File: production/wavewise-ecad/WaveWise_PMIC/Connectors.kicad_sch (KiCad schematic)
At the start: 32 parts, among them J1 24V output, J10 5031590200, J11 5031590200, J13 Screw_Terminal_01x03, J2 Conn_01x06_Pin, J3 Conn_01x03_Pin, J5 5031590400, J6 5031590400, J8 5031590800, J9 5031590300

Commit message: fix drc
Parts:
- removed J1: 24V output, Unchecked:2pinmolex, symbol Connector:Screw_Terminal_01x02
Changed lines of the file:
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@@
-    (stroke (width 0) (type default))
-  )
-  (wire (pts (xy 67.31 113.665) (xy 69.215 113.665))
     (stroke (width 0) (type default))
   )
@@
   )
   (wire (pts (xy 68.58 27.94) (xy 80.645 27.94))
-    (stroke (width 0) (type default))
-  )
-  (wire (pts (xy 67.31 111.125) (xy 73.025 111.125))
     (stroke (width 0) (type default))
   )
@@
     )
   )
-  (symbol (lib_id "power:GND") (at 69.215 113.665 0) (unit 1)
-    (in_bom yes) (on_board yes) (dnp no)
-    (property "Reference" "#PWR03" (at 69.215 120.015 0)
-      (effects (font (size 1.27 1.27)) hide)
-    )
-    (property "Value" "GND" (at 72.39 114.3 0)
-      (effects (font (size 1.27 1.27)))
-    )
-    (property "Footprint" "" (at 69.215 113.665 0)
-      (effects (font (size 1.27 1.27)) hide)
-    )
-    (property "Datasheet" "" (at 69.215 113.665 0)
-      (effects (font (size 1.27 1.27)) hide)
-    )
-    (pin "1")
-    (instances
-      (project "WaveWise_PMIC"
-        (path "/8343c01b-8940-4cb8-a17d-91fd7fb1cccd/7fd42481-dc5a-4ae0-adec-c5e7a3228be9"
-          (reference "#PWR03") (unit 1)
-        )
-      )
-    )
-  )
   (symbol (lib_id "power:GND") (at 97.79 148.59 0) (unit 1)
     (in_bom yes) (on_board yes) (dnp no) (fields_autoplaced)
@@
         (path "/8343c01b-8940-4cb8-a17d-91fd7fb1cccd/7fd42481-dc5a-4ae0-adec-c5e7a3228be9"
           (reference "#PWR055") (unit 1)
-        )
-      )
-    )
-  )
-  (symbol (lib_id "Connector:Screw_Terminal_01x02") (at 62.23 113.665 180) (unit 1)
-    (in_bom yes) (on_board yes) (dnp no) (fields_autoplaced)
-    (property "Reference" "J1" (at 62.23 105.41 0)
-      (effects (font (size 1.27 1.27)))
-    )
-    (property "Value" "24V output" (at 62.23 107.95 0)
-      (effects (font (size 1.27 1.27)))
-    )
-    (property "Footprint" "Unchecked:2pinmolex" (at 62.23 113.665 0)
-      (effects (font (size 1.27 1.27)) hide)
-    )
-    (property "Datasheet" "~" (at 62.23 113.665 0)
-      (effects (font (size 1.27 1.27)) hide)
-    )
-    (pin "1")
-    (pin "2")
-    (instances
-      (project "WaveWise_PMIC"
-        (path "/8343c01b-8940-4cb8-a17d-91fd7fb1cccd/7fd42481-dc5a-4ae0-adec-c5e7a3228be9"
-          (reference "J1") (unit 1)
         )
       )
@@
         )
       )
-    )
-  )
-  (symbol (lib_id "power:+24V") (at 73.025 111.125 0) (unit 1)
-    (in_bom yes) (on_board yes) (dnp no) (fields_autoplaced)
-    (property "Reference" "#PWR01" (at 73.025 114.935 0)
-      (effects (font (size 1.27 1.27)) hide)
-    )
-    (property "Value" "+24V" (at 73.025 106.045 0)
-      (effects (font (size 1.27 1.27)))
-    )
-    (property "Footprint" "" (at 73.025 111.125 0)
-      (effects (font (size 1.27 1.27)) hide)
-    )
-    (property "Datasheet" "" (at 73.025 111.125 0)
-      (effects (font (size 1.27 1.27)) hide)
-    )
-    (pin "1")
-    (instances
-      (project "WaveWise_PMIC"
-        (path "/8343c01b-8940-4cb8-a17d-91fd7fb1cccd/7fd42481-dc5a-4ae0-adec-c5e7a3228be9"
-          (reference "#PWR01") (unit 1)
-        )
-      )

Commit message: power stuff
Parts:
- removed R25, R26: 0, Resistor_SMD:R_0805_2012Metric, symbol Device:R
- J5: footprint Unchecked:4pinmolex -> Connector_Molex:Molex_Micro-Fit_3.0_43650-0400_1x04_P3.00mm_Horizontal
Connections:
- net Inverter_Input: now also J13.2 (Pin_2)
- net air_comp_dio renamed SICO_PUMP_CONTROL
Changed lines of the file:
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@@
   (junction (at 50.8 136.144) (diameter 0) (color 0 0 0 0)
-  )
-  (junction (at 44.45 63.5) (diameter 0) (color 0 0 0 0)
   )
   (junction (at 157.48 106.68) (diameter 0) (color 0 0 0 0)
@@
     (stroke (width 0) (type default))
   )
-  (wire (pts (xy 44.45 62.23) (xy 44.45 63.5))
-    (stroke (width 0) (type default))
-  )
   (wire (pts (xy 157.48 111.76) (xy 157.48 106.68))
     (stroke (width 0) (type default))
@@
     (stroke (width 0.15) (type dash))
   )
-  (wire (pts (xy 27.94 63.5) (xy 44.45 63.5))
+  (wire (pts (xy 27.94 63.5) (xy 34.29 63.5))
     (stroke (width 0) (type default))
   )
@@
   )
   (wire (pts (xy 67.31 62.23) (xy 80.01 62.23))
-    (stroke (width 0) (type default))
-  )
-  (wire (pts (xy 44.45 63.5) (xy 44.45 67.31))
     (stroke (width 0) (type default))
   )
@@
     )
   )
-  (global_label "air_comp_dio" (shape input) (at 127 33.02 180) (fields_autoplaced)
-    (effects (font (size 1.27 1.27)) (justify right))
-    (property "Intersheetrefs" "${INTERSHEET_REFS}" (at 111.5569 33.02 0)
-      (effects (font (size 1.27 1.27)) (justify right) hide)
-    )
-  )
-  (global_label "air_comp_dio" (shape input) (at 44.45 74.93 270) (fields_autoplaced)
-    (effects (font (size 1.27 1.27)) (justify right))
-    (property "Intersheetrefs" "${INTERSHEET_REFS}" (at 44.45 90.3731 90)
-      (effects (font (size 1.27 1.27)) (justify right) hide)
-    )
-  )
   (global_label "panel_sense" (shape input) (at 120.904 88.9 180) (fields_autoplaced)
     (effects (font (size 1.27 1.27)) (justify right))
@@
     (effects (font (size 1.27 1.27)) (justify left))
   )
-  (hierarchical_label "Inverter_Input" (shape input) (at 44.45 54.61 90) (fields_autoplaced)
+  (hierarchical_label "Inverter_Input" (shape input) (at 34.29 63.5 0) (fields_autoplaced)
     (effects (font (size 1.27 1.27)) (justify left))
   )
   (hierarchical_label "BATT_SENSE_DIO" (shape input) (at 135.128 63.754 0) (fields_autoplaced)
     (effects (font (size 1.27 1.27)) (justify left))
+  )
+  (hierarchical_label "SICO_PUMP_CONTROL" (shape input) (at 127 33.02 180) (fields_autoplaced)
+    (effects (font (size 1.27 1.27)) (justify right))
   )
   (hierarchical_label "SWDIO" (shape input) (at 34.29 151.13 0) (fields_autoplaced)
@@
     )
   )
-  (symbol (lib_id "power:+5V") (at 40.64 36.83 270) (unit 1)
-    (in_bom yes) (on_board yes) (dnp no) (fields_autoplaced)
-    (property "Reference" "#PWR04" (at 36.83 36.83 0)
-      (effects (font (size 1.27 1.27)) hide)
-    )
-    (property "Value" "+5V" (at 44.45 36.83 90)
-      (effects (font (size 1.27 1.27)) (justify left))
-    )
-    (property "Footprint" "" (at 40.64 36.83 0)
-      (effects (font (size 1.27 1.27)) hide)
-    )
-    (property "Datasheet" "" (at 40.64 36.83 0)
-      (effects (font (size 1.27 1.27)) hide)
-    )
-    (pin "1")
-    (instances
-      (project "WaveWise_PMIC"
-        (path "/8343c01b-8940-4cb8-a17d-91fd7fb1cccd/7fd42481-dc5a-4ae0-adec-c5e7a3228be9"
-          (reference "#PWR04") (unit 1)
-        )
-      )
-    )
-  )
   (symbol (lib_id "2pinmolex:5031590200") (at 31.75 104.14 180) (unit 1)
     (in_bom yes) (on_board yes) (dnp no) (fields_autoplaced)
@@
     )
   )
-  (symbol (lib_id "Device:R") (at 44.45 58.42 180) (unit 1)
-    (in_bom yes) (on_board yes) (dnp yes) (fields_autoplaced)
-    (property "Reference" "R26" (at 46.99 57.15 0)
-      (effects (font (size 1.27 1.27)) (justify right))
-    )
-    (property "Value" "0" (at 46.99 59.69 0)
-      (effects (font (size 1.27 1.27)) (justify right))
-    )
-    (property "Footprint" "Resistor_SMD:R_0805_2012Metric" (at 46.228 58.42 90)
-      (effects (font (size 1.27 1.27)) hide)
-    )
-    (property "Datasheet" "~" (at 44.45 58.42 0)
-      (effects (font (size 1.27 1.27)) hide)
-    )
-    (pin "1")
-    (pin "2")
-    (instances
-      (project "WaveWise_PMIC"
-        (path "/8343c01b-8940-4cb8-a17d-91fd7fb1cccd/7fd42481-dc5a-4ae0-adec-c5e7a3228be9"
-          (reference "R26") (unit 1)
-        )
-      )
-    )
-  )
   (symbol (lib_id "power:GND") (at 27.94 66.04 0) (unit 1)
     (in_bom yes) (on_board yes) (dnp no) (fields_autoplaced)
@@
       (effects (font (size 1.524 1.524)))
     )
-    (property "Footprint" "Unchecked:4pinmolex" (at 29.21 132.08 0)
+    (property "Footprint" "Connector_Molex:Molex_Micro-Fit_3.0_43650-0400_1x04_P3.00mm_Horizontal" (at 29.21 132.08 0)
       (effects (font (size 1.27 1.27) italic) hide)
     )
@@
     )
   )
-  (symbol (lib_id "Device:R") (at 44.45 71.12 180) (unit 1)
-    (in_bom yes) (on_board yes) (dnp no) (fields_autoplaced)
-    (property "Reference" "R25" (at 46.99 69.85 0)
-      (effects (font (size 1.27 1.27)) (justify right))
-    )
-    (property "Value" "0" (at 46.99 72.39 0)
-      (effects (font (size 1.27 1.27)) (justify right))
-    )
-    (property "Footprint" "Resistor_SMD:R_0805_2012Metric" (at 46.228 71.12 90)
-      (effects (font (size 1.27 1.27)) hide)
-    )
-    (property "Datasheet" "~" (at 44.45 71.12 0)
-      (effects (font (size 1.27 1.27)) hide)
-    )
-    (pin "1")
-    (pin "2")
-    (instances
-      (project "WaveWise_PMIC"
-        (path "/8343c01b-8940-4cb8-a17d-91fd7fb1cccd/7fd42481-dc5a-4ae0-adec-c5e7a3228be9"
-          (reference "R25") (unit 1)
-        )
-      )
+  (symbol (lib_id "power:+5V") (at 40.64 36.83 270) (unit 1)
+    (in_bom yes) (on_board yes) (dnp no) (fields_autoplaced)
+    (property "Reference" "#PWR01" (at 36.83 36.83 0)
+      (effects (font (size 1.27 1.27)) hide)
+    )
+    (property "Value" "+5V" (at 44.45 36.83 90)
+      (effects (font (size 1.27 1.27)) (justify left))
+    )
+    (property "Footprint" "" (at 40.64 36.83 0)
+      (effects (font (size 1.27 1.27)) hide)
+    )
+    (property "Datasheet" "" (at 40.64 36.83 0)
+      (effects (font (size 1.27 1.27)) hide)
+    )
+    (pin "1")
+    (instances
+      (project "WaveWise_PMIC"
+        (path "/8343c01b-8940-4cb8-a17d-91fd7fb1cccd/7fd42481-dc5a-4ae0-adec-c5e7a3228be9"
+          (reference "#PWR01") (unit 1)
+        )
+      )

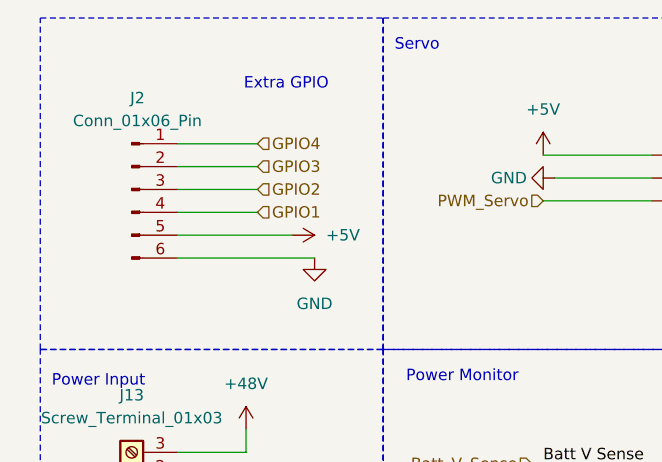
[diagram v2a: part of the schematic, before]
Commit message: change pins on pico for layout
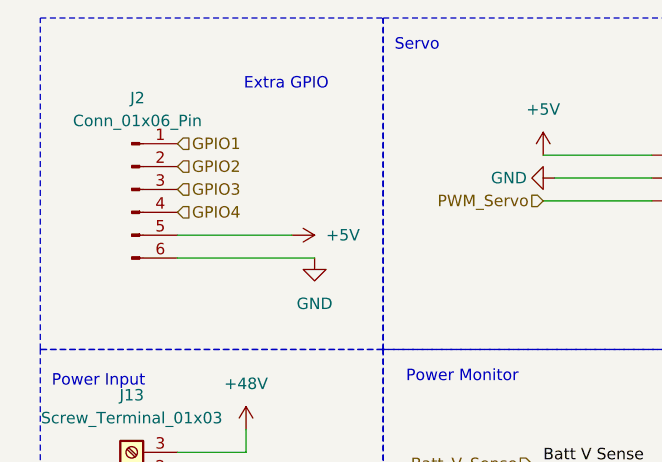
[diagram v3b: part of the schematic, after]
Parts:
- J10, J11: footprint Unchecked:2pinmolex -> Connector_Molex:Molex_MicroClasp_55932-0210_1x02_P2.00mm_Vertical
- J6: footprint Unchecked:4pinmolex -> Connector_Molex:Molex_MicroClasp_55932-0410_1x04_P2.00mm_Vertical
- J8: footprint Unchecked:8pinmolex -> Connector_Molex:Molex_MicroClasp_55932-0810_1x08_P2.00mm_Vertical
- J9: footprint Unchecked:3pinmolex -> Connector_Molex:Molex_MicroClasp_55932-0310_1x03_P2.00mm_Vertical
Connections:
- net GPIO1: now also J2.1 (Pin_1); no longer J2.4 (Pin_4)
- net GPIO2: now also J2.2 (Pin_2); no longer J2.3 (Pin_3)
- net GPIO3: now also J2.3 (Pin_3); no longer J2.2 (Pin_2)
- net GPIO4: now also J2.4 (Pin_4); no longer J2.1 (Pin_1)
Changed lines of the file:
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@@
   (junction (at 157.48 106.68) (diameter 0) (color 0 0 0 0)
-  )
-  (wire (pts (xy 27.94 26.67) (xy 36.83 26.67))
-    (stroke (width 0) (type default))
   )
   (polyline (pts (xy 105.41 123.19) (xy 105.41 126.746))
@@
     (stroke (width 0) (type default))
   )
-  (wire (pts (xy 27.94 31.75) (xy 36.83 31.75))
-    (stroke (width 0) (type default))
-  )
   (wire (pts (xy 124.714 22.098) (xy 124.714 22.86))
     (stroke (width 0) (type default))
@@
     (stroke (width 0) (type default))
   )
-  (wire (pts (xy 27.94 34.29) (xy 36.83 34.29))
-    (stroke (width 0) (type default))
-  )
   (wire (pts (xy 172.72 106.68) (xy 176.53 106.68))
     (stroke (width 0) (type default))
@@
   )
   (wire (pts (xy 120.904 92.71) (xy 128.27 92.71))
-    (stroke (width 0) (type default))
-  )
-  (wire (pts (xy 27.94 29.21) (xy 36.83 29.21))
     (stroke (width 0) (type default))
   )
@@
     )
   )
-  (hierarchical_label "GPIO4" (shape input) (at 36.83 26.67 0) (fields_autoplaced)
+  (hierarchical_label "GPIO4" (shape input) (at 27.94 34.29 0) (fields_autoplaced)
     (effects (font (size 1.27 1.27)) (justify left))
   )
@@
     (effects (font (size 1.27 1.27)) (justify left))
   )
-  (hierarchical_label "GPIO1" (shape input) (at 36.83 34.29 0) (fields_autoplaced)
+  (hierarchical_label "GPIO1" (shape input) (at 27.94 26.67 0) (fields_autoplaced)
     (effects (font (size 1.27 1.27)) (justify left))
   )
-  (hierarchical_label "GPIO3" (shape input) (at 36.83 29.21 0) (fields_autoplaced)
+  (hierarchical_label "GPIO3" (shape input) (at 27.94 31.75 0) (fields_autoplaced)
     (effects (font (size 1.27 1.27)) (justify left))
   )
@@
     (effects (font (size 1.27 1.27)) (justify left))
   )
-  (hierarchical_label "GPIO2" (shape input) (at 36.83 31.75 0) (fields_autoplaced)
+  (hierarchical_label "GPIO2" (shape input) (at 27.94 29.21 0) (fields_autoplaced)
     (effects (font (size 1.27 1.27)) (justify left))
   )
@@
       (effects (font (size 1.524 1.524)))
     )
-    (property "Footprint" "Unchecked:2pinmolex" (at 31.75 104.14 0)
+    (property "Footprint" "Connector_Molex:Molex_MicroClasp_55932-0210_1x02_P2.00mm_Vertical" (at 31.75 104.14 0)
       (effects (font (size 1.27 1.27) italic) hide)
     )
@@
       (effects (font (size 1.524 1.524)))
     )
-    (property "Footprint" "Unchecked:4pinmolex" (at 125.73 116.84 0)
+    (property "Footprint" "Connector_Molex:Molex_MicroClasp_55932-0410_1x04_P2.00mm_Vertical" (at 125.73 116.84 0)
       (effects (font (size 1.27 1.27) italic) hide)
     )
@@
       (effects (font (size 1.524 1.524)) (justify left))
     )
-    (property "Footprint" "Unchecked:8pinmolex" (at 127 22.86 0)
+    (property "Footprint" "Connector_Molex:Molex_MicroClasp_55932-0810_1x08_P2.00mm_Vertical" (at 127 22.86 0)
       (effects (font (size 1.27 1.27) italic) hide)
     )
@@
       (effects (font (size 1.524 1.524)))
     )
-    (property "Footprint" "Unchecked:2pinmolex" (at 31.115 85.725 0)
+    (property "Footprint" "Connector_Molex:Molex_MicroClasp_55932-0210_1x02_P2.00mm_Vertical" (at 31.115 85.725 0)
       (effects (font (size 1.27 1.27) italic) hide)
     )
@@
       (effects (font (size 1.524 1.524)) (justify left))
     )
-    (property "Footprint" "Unchecked:3pinmolex" (at 80.645 27.94 0)
+    (property "Footprint" "Connector_Molex:Molex_MicroClasp_55932-0310_1x03_P2.00mm_Vertical" (at 80.645 27.94 0)
       (effects (font (size 1.27 1.27) italic) hide)
     )

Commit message: add back in 24V output
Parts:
- added J1: 5031590200, Connector_Molex:Molex_MicroClasp_55932-0210_1x02_P2.00mm_Vertical, symbol 2pinmolex:5031590200
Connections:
- net +24V: now also J1.2
- net GND: now also J1.1
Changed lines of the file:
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@@
     (stroke (width 0.15) (type dash))
+  )
+  (wire (pts (xy 71.12 100.33) (xy 78.74 100.33))
+    (stroke (width 0) (type default))
   )
   (wire (pts (xy 27.94 63.5) (xy 34.29 63.5))
@@
     (stroke (width 0) (type default))
   )
+  (wire (pts (xy 71.12 102.87) (xy 74.93 102.87))
+    (stroke (width 0) (type default))
+  )
   (wire (pts (xy 35.56 58.42) (xy 35.56 60.96))
     (stroke (width 0) (type default))
@@
   )
   (wire (pts (xy 38.735 80.645) (xy 38.735 83.185))
+    (stroke (width 0) (type default))
+  )
+  (wire (pts (xy 78.74 97.79) (xy 78.74 100.33))
     (stroke (width 0) (type default))
   )
@@
         (path "/8343c01b-8940-4cb8-a17d-91fd7fb1cccd/7fd42481-dc5a-4ae0-adec-c5e7a3228be9"
           (reference "#PWR01") (unit 1)
+        )
+      )
+    )
+  )
+  (symbol (lib_id "2pinmolex:5031590200") (at 71.12 102.87 180) (unit 1)
+    (in_bom yes) (on_board yes) (dnp no) (fields_autoplaced)
+    (property "Reference" "J1" (at 62.23 93.345 0)
+      (effects (font (size 1.524 1.524)))
+    )
+    (property "Value" "5031590200" (at 62.23 95.885 0)
+      (effects (font (size 1.524 1.524)))
+    )
+    (property "Footprint" "Connector_Molex:Molex_MicroClasp_55932-0210_1x02_P2.00mm_Vertical" (at 71.12 102.87 0)
+      (effects (font (size 1.27 1.27) italic) hide)
+    )
+    (property "Datasheet" "5031590200" (at 71.12 102.87 0)
+      (effects (font (size 1.27 1.27) italic) hide)
+    )
+    (pin "2")
+    (pin "1")
+    (instances
+      (project "WaveWise_PMIC"
+        (path "/8343c01b-8940-4cb8-a17d-91fd7fb1cccd/7fd42481-dc5a-4ae0-adec-c5e7a3228be9"
+          (reference "J1") (unit 1)
         )
       )
@@
     )
   )
+  (symbol (lib_id "power:GND") (at 74.93 102.87 0) (unit 1)
+    (in_bom yes) (on_board yes) (dnp no) (fields_autoplaced)
+    (property "Reference" "#PWR03" (at 74.93 109.22 0)
+      (effects (font (size 1.27 1.27)) hide)
+    )
+    (property "Value" "GND" (at 74.93 107.95 0)
+      (effects (font (size 1.27 1.27)))
+    )
+    (property "Footprint" "" (at 74.93 102.87 0)
+      (effects (font (size 1.27 1.27)) hide)
+    )
+    (property "Datasheet" "" (at 74.93 102.87 0)
+      (effects (font (size 1.27 1.27)) hide)
+    )
+    (pin "1")
+    (instances
+      (project "WaveWise_PMIC"
+        (path "/8343c01b-8940-4cb8-a17d-91fd7fb1cccd/7fd42481-dc5a-4ae0-adec-c5e7a3228be9"
+          (reference "#PWR03") (unit 1)
+        )
+      )
+    )
+  )
   (symbol (lib_id "power:GND") (at 116.84 148.59 0) (unit 1)
     (in_bom yes) (on_board yes) (dnp no) (fields_autoplaced)
@@
         )
       )
+    )
+  )
+  (symbol (lib_id "power:+24V") (at 78.74 97.79 0) (unit 1)
+    (in_bom yes) (on_board yes) (dnp no) (fields_autoplaced)
+    (property "Reference" "#PWR04" (at 78.74 101.6 0)
+      (effects (font (size 1.27 1.27)) hide)
+    )
+    (property "Value" "+24V" (at 78.74 92.71 0)
+      (effects (font (size 1.27 1.27)))
+    )
+    (property "Footprint" "" (at 78.74 97.79 0)
+      (effects (font (size 1.27 1.27)) hide)
+    )
+    (property "Datasheet" "" (at 78.74 97.79 0)
+      (effects (font (size 1.27 1.27)) hide)
+    )
+    (pin "1")
+    (instances
+      (project "WaveWise_PMIC"
+        (path "/8343c01b-8940-4cb8-a17d-91fd7fb1cccd/7fd42481-dc5a-4ae0-adec-c5e7a3228be9"
+          (reference "#PWR04") (unit 1)
+        )
+      )

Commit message: change 24V from microclasp to microfit
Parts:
- J1: footprint Connector_Molex:Molex_MicroClasp_55932-0210_1x02_P2.00mm_Vertical -> Connector_Molex:Molex_Micro-Fit_3.0_43650-0215_1x02_P3.00mm_Vertical
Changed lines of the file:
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@@
       (effects (font (size 1.524 1.524)))
     )
-    (property "Footprint" "Connector_Molex:Molex_MicroClasp_55932-0210_1x02_P2.00mm_Vertical" (at 71.12 102.87 0)
+    (property "Footprint" "Connector_Molex:Molex_Micro-Fit_3.0_43650-0215_1x02_P3.00mm_Vertical" (at 71.12 102.87 0)
       (effects (font (size 1.27 1.27) italic) hide)
     )
